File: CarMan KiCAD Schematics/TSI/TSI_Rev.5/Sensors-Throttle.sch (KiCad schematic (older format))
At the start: 56 parts, among them IC1 TS431ILT, J13 Conn_01x01, J22 Conn_01x01, J23 Conn_01x01, J24 Conn_01x01, J25 Conn_01x01, J26 J26, U21 MCP6004, U25 NCD9830DBR2G, U26 MCP6004, U4 ACPL-C870, U40 MCP6004, U5 SI8600AB-B-IS

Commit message: TSI Footprints - Res, Caps, Inductor all 0805s - Mounting Holes
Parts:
- C20, C21, C30, C32, C35, C4, C43, C46, C47, C48, C9: footprint (none) -> Capacitor_SMD:C_0805_2012Metric_Pad1.15x1.40mm_HandSolder
- R10, R103, R13, R16, R50, R51, R53, R58, R59, R6, R62, R63, R64, R66, R7, R76, R77, R78, R84, R85, R86, R87, R88, R89, R9, R90, R91, R93, R94, R95, R96: footprint (none) -> Resistor_SMD:R_0805_2012Metric_Pad1.15x1.40mm_HandSolder
- U40: footprint (none) -> TSI_Rev_2021_Footprint_Lib:SOIC127P600X175-14N

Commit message: TSI Footprinting (~80%)  - Added Molex  - Added Current Sensor
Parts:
- J13, J23, J24, J25, J26: footprint (none) -> Connector_PinHeader_1.00mm:PinHeader_1x01_P1.00mm_Vertical
- J22: value Conn_01x01 -> J22; footprint (none) -> Connector_PinHeader_1.00mm:PinHeader_1x01_P1.00mm_Vertical
- TP8: footprint (none) -> TestPoint:TestPoint_Pad_D3.0mm
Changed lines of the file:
@@
 F 0 "J24" V 14350 5650 50  0000 L CNN
 F 1 "Conn_01x01" V 14350 5500 50  0001 L CNN
-F 2 "" H 14250 5700 50  0001 C CNN
+F 2 "Connector_PinHeader_1.00mm:PinHeader_1x01_P1.00mm_Vertical" H 14250 5700 50  0001 C CNN
 F 3 "~" H 14250 5700 50  0001 C CNN
 	1    14250 5700
@@
 F 0 "J23" V 14350 4750 50  0000 L CNN
 F 1 "Conn_01x01" V 14213 4880 50  0001 L CNN
-F 2 "" H 14250 4800 50  0001 C CNN
+F 2 "Connector_PinHeader_1.00mm:PinHeader_1x01_P1.00mm_Vertical" H 14250 4800 50  0001 C CNN
 F 3 "~" H 14250 4800 50  0001 C CNN
 	1    14250 4800
@@
 F 0 "J25" V 14350 6450 50  0000 L CNN
 F 1 "Conn_01x01" V 14350 6300 50  0001 L CNN
-F 2 "" H 14250 6500 50  0001 C CNN
+F 2 "Connector_PinHeader_1.00mm:PinHeader_1x01_P1.00mm_Vertical" H 14250 6500 50  0001 C CNN
 F 3 "~" H 14250 6500 50  0001 C CNN
 	1    14250 6500
@@
 P 12800 6500
 F 0 "J22" V 12900 6450 50  0000 L CNN
-F 1 "Conn_01x01" V 12900 6300 50  0001 L CNN
-F 2 "" H 12800 6500 50  0001 C CNN
+F 1 "J22" V 12900 6300 50  0001 L CNN
+F 2 "Connector_PinHeader_1.00mm:PinHeader_1x01_P1.00mm_Vertical" H 12800 6500 50  0001 C CNN
 F 3 "~" H 12800 6500 50  0001 C CNN
 	1    12800 6500
@@
 F 0 "J26" V 12900 5650 50  0000 L CNN
 F 1 "J26" V 12900 5500 50  0001 L CNN
-F 2 "" H 12800 5700 50  0001 C CNN
+F 2 "Connector_PinHeader_1.00mm:PinHeader_1x01_P1.00mm_Vertical" H 12800 5700 50  0001 C CNN
 F 3 "~" H 12800 5700 50  0001 C CNN
 	1    12800 5700
@@
 F 0 "J13" V 12900 4750 50  0000 L CNN
 F 1 "Conn_01x01" V 12900 4600 50  0001 L CNN
-F 2 "" H 12800 4800 50  0001 C CNN
+F 2 "Connector_PinHeader_1.00mm:PinHeader_1x01_P1.00mm_Vertical" H 12800 4800 50  0001 C CNN
 F 3 "~" H 12800 4800 50  0001 C CNN
 	1    12800 4800
@@
 F 0 "TP8" H 6850 2050 50  0000 L CNN
 F 1 "Throttle_HV" H 6600 2250 50  0000 L CNN
-F 2 "" H 7000 2000 50  0001 C CNN
+F 2 "TestPoint:TestPoint_Pad_D3.0mm" H 7000 2000 50  0001 C CNN
 F 3 "~" H 7000 2000 50  0001 C CNN
 	1    6800 2000

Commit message: Started TSI PCB
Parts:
- removed unit 1 of U26
- added unit 4 of U26
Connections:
- net MC_Voltage: now also U21.7; no longer U21.1
- net TSV_Voltage: now also U21.1; no longer U21.7
- net at R95.1: now also U26.13 (-), U26.14
- net at C4.1, J13.1 (Pin_1), R6.2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: now also U26.12 (+)
- net at R95.2: now also U21.6 (-); no longer U21.2 (-)
- net at R89.1, R96.2: now also U21.5 (+); no longer U21.3 (+)
- net at R91.2, R93.2: now also U21.3 (+); no longer U21.5 (+)
- net at R90.1, R94.2: now also U21.2 (-); no longer U21.6 (-)
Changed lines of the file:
@@
 $Descr A3 16535 11693
 encoding utf-8
-Sheet 6 6
+Sheet 5 6
 Title ""
 Date ""
@@
 Wire Wire Line
 	10900 4300 11000 4300
-Text Notes 11700 4200 2    55   ~ 0
+Text Notes 11600 4150 2    55   ~ 0
 Bypass Cap for U26\n\n
 Wire Wire Line
@@
 $Comp
 L Amplifier_Operational:MCP6004 U21
-U 1 1 5F995327
+U 2 1 5F995327
 P 10000 5100
 F 0 "U21" H 10000 5100 50  0000 C CNN
@@
 F 2 "TSI_Rev_2021_Footprint_Lib:SOIC127P600X175-14N" H 9950 5200 50  0001 C CNN
 F 3 "http://ww1.microchip.com/downloads/en/DeviceDoc/21733j.pdf" H 10050 5300 50  0001 C CNN
-	1    10000 5100
+	2    10000 5100
 	-1   0    0    1
 $EndComp
@@
 $Comp
 L Amplifier_Operational:MCP6004 U21
-U 2 1 5F995FD0
+U 1 1 5F995FD0
 P 10000 6300
 F 0 "U21" H 10000 6300 50  0000 C CNN
@@
 F 2 "TSI_Rev_2021_Footprint_Lib:SOIC127P600X175-14N" H 9950 6400 50  0001 C CNN
 F 3 "http://ww1.microchip.com/downloads/en/DeviceDoc/21733j.pdf" H 10050 6500 50  0001 C CNN
-	2    10000 6300
+	1    10000 6300
 	-1   0    0    -1
 $EndComp
@@
 Text HLabel 2100 9200 0    50   Input ~ 0
 Throttle_LV
-Text HLabel 5950 9700 2    50   Output ~ 0
+Text HLabel 5950 9750 2    50   Output ~ 0
 1.24V_REF
 Text HLabel 5750 8800 0    50   Input ~ 0
@@
 Text HLabel 5750 8700 0    50   Input ~ 0
 5HV
-Text HLabel 5750 9300 0    50   Input ~ 0
+Text HLabel 5750 9400 0    50   Input ~ 0
 Throttle_HV
 Wire Wire Line
@@
 IO_Ground
 Wire Wire Line
-	5950 9300 5750 9300
-Text Label 5950 9300 0    50   ~ 0
+	5950 9400 5750 9400
+Text Label 5950 9400 0    50   ~ 0
 Throttle_HV
 Wire Wire Line
 	5950 8700 5750 8700
 Wire Wire Line
-	5950 9700 5750 9700
-Text Label 5750 9700 2    50   ~ 0
+	5950 9750 5750 9750
+Text Label 5750 9750 2    50   ~ 0
 DiffAmp_REF
 Text Label 5950 8700 0    50   ~ 0
@@
 Text Notes 5150 8550 0    79   ~ 0
 HIGH VOLTAGE SIGNALS\n
+Text Label 5950 9200 0    50   ~ 0
+HV+
+Wire Wire Line
+	5950 9200 5750 9200
+Text Label 5950 8900 0    50   ~ 0
+TSV_Voltage
 Text Label 5950 9100 0    50   ~ 0
+MC+
+Wire Wire Line
+	5950 9100 5750 9100
+Wire Wire Line
+	5950 8900 5750 8900
+Text HLabel 5750 8900 0    50   Input ~ 0
+TSV_Voltage
+Text HLabel 5750 9100 0    50   Input ~ 0
+MC+
+Text HLabel 5750 9200 0    50   Input ~ 0
 HV+
-Wire Wire Line
-	5950 9100 5750 9100
-Text Label 5950 9000 0    50   ~ 0
-TSV_Voltage
-Text Label 5950 8900 0    50   ~ 0
-MC_Voltage
-Wire Wire Line
-	5950 8900 5750 8900
-Wire Wire Line
-	5950 9000 5750 9000
-Text HLabel 5750 9000 0    50   Input ~ 0
-TSV_Voltage
-Text HLabel 5750 8900 0    50   Input ~ 0
-MC_Voltage
-Text HLabel 5750 9100 0    50   Input ~ 0
-HV+
-Text Label 5950 9200 0    50   ~ 0
+Text Label 5950 9300 0    50   ~ 0
 HV-
 Wire Wire Line
-	5950 9200 5750 9200
-Text HLabel 5750 9200 0    50   Input ~ 0
+	5950 9300 5750 9300
+Text HLabel 5750 9300 0    50   Input ~ 0
 HV-
 Wire Notes Line
@@
 Text Notes 12100 10450 0    157  ~ 0
 V/I\n& THROTTLE VOLTAGE ISOLATOR
+Text Label 5950 9600 0    50   ~ 0
+A2_HV
 Text Label 5950 9500 0    50   ~ 0
+A1_HV
+Wire Wire Line
+	5950 9600 5750 9600
+Wire Wire Line
+	5950 9500 5750 9500
+Text HLabel 5750 9500 0    50   Input ~ 0
+A1_HV
+Text HLabel 5750 9600 0    50   Input ~ 0
 A2_HV
-Text Label 5950 9400 0    50   ~ 0
-A1_HV
-Wire Wire Line
-	5950 9500 5750 9500
-Wire Wire Line
-	5950 9400 5750 9400
-Text HLabel 5750 9400 0    50   Input ~ 0
-A1_HV
-Text HLabel 5750 9500 0    50   Input ~ 0
-A2_HV
-Wire Notes Line
-	5050 9800 6650 9800
+Wire Notes Line
+	5050 9850 6650 9850
 Wire Notes Line
 	5050 8350 5050 9800
@@
 Wire Notes Line
 	6650 8350 6650 9800
-$Comp
-L Amplifier_Operational:MCP6004 U26
-U 1 1 5F98F236
-P 11500 4700
-F 0 "U26" H 11500 4700 50  0000 C CNN
-F 1 "MCP6004" H 11650 4850 50  0000 C CNN
-F 2 "TSI_Rev_2021_Footprint_Lib:SOIC127P600X175-14N" H 11450 4800 50  0001 C CNN
-F 3 "http://ww1.microchip.com/downloads/en/DeviceDoc/21733j.pdf" H 11550 4900 50  0001 C CNN
-	1    11500 4700
-	-1   0    0    -1
-$EndComp
 $Comp
 L Amplifier_Operational:MCP6004 U26
@@
 Wire Wire Line
 	3300 1350 3200 1350
+Text Label 5950 9000 0    50   ~ 0
+MC_Voltage
+Wire Wire Line
+	5950 9000 5750 9000
+Text HLabel 5750 9000 0    50   Input ~ 0
+MC_Voltage
+$Comp
+L Amplifier_Operational:MCP6004 U26
+U 4 1 601D0B35
+P 11500 4700
+F 0 "U26" H 11450 4700 50  0000 C CNN
+F 1 "MCP6004" H 11650 4850 50  0000 C CNN
+F 2 "TSI_Rev_2021_Footprint_Lib:SOIC127P600X175-14N" H 11450 4800 50  0001 C CNN
+F 3 "http://ww1.microchip.com/downloads/en/DeviceDoc/21733j.pdf" H 11550 4900 50  0001 C CNN
+	4    11500 4700
+	-1   0    0    -1
+$EndComp
 $EndSCHEMATC

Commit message: TSI (~97%)
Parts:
- J27: renamed from J22; value J22 -> J27
- renumbered J23 to J28
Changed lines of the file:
@@
 	14250 5500 14200 5500
 $Comp
-L Connector_Generic:Conn_01x01 J23
+L Connector_Generic:Conn_01x01 J28
 U 1 1 5FA1321C
 P 14250 4800
-F 0 "J23" V 14350 4750 50  0000 L CNN
+F 0 "J28" V 14350 4750 50  0000 L CNN
 F 1 "Conn_01x01" V 14213 4880 50  0001 L CNN
 F 2 "Connector_PinHeader_1.00mm:PinHeader_1x01_P1.00mm_Vertical" H 14250 4800 50  0001 C CNN
@@
 $EndComp
 $Comp
-L Connector_Generic:Conn_01x01 J22
+L Connector_Generic:Conn_01x01 J27
 U 1 1 5FA19A24
 P 12800 6500
-F 0 "J22" V 12900 6450 50  0000 L CNN
-F 1 "J22" V 12900 6300 50  0001 L CNN
+F 0 "J27" V 12900 6450 50  0000 L CNN
+F 1 "J27" V 12900 6300 50  0001 L CNN
 F 2 "Connector_PinHeader_1.00mm:PinHeader_1x01_P1.00mm_Vertical" H 12800 6500 50  0001 C CNN
 F 3 "~" H 12800 6500 50  0001 C CNN

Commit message: Aesthetics
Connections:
- net 5HV: now also U25.10 (REF_IN/REF_OUT)
- no-connect marks 7 -> 6
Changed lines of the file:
@@
 Text Label 8200 5550 0    50   ~ 0
 A1_HV
-NoConn ~ 6850 5250
 Wire Wire Line
 	6750 6000 6850 6000
@@
 	-1   0    0    -1
 $EndComp
+Text Label 6550 5250 0    50   ~ 0
+5HV
+Wire Wire Line
+	6550 5250 6850 5250
 $EndSCHEMATC

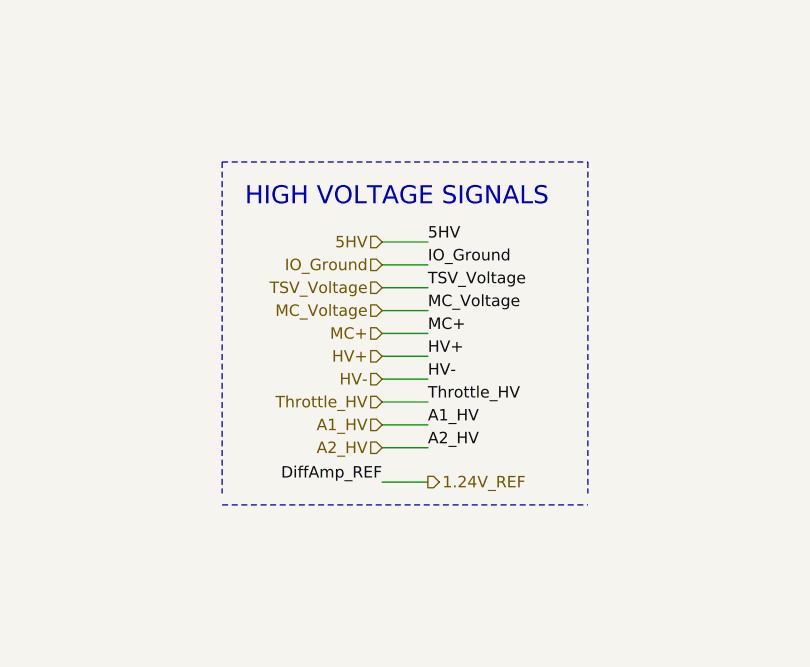
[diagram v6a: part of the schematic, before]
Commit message: TSI Signal Review ISSUES: - PCDC 'Pre_Charge_Ready' and 'PC_Ready' discrepancy - TSI Rev.4 IC1, IC4 -> PCDC & Isolators
REMOVED SIGNALS:
Throttle Plausibility
 - PC_Ready
 - Drive_BTN
 PCDC
 - HV+
 - HV-
 - Throttle_HV
 - IGNI_GND

STATUS LIGHTS & COCKPIT
- BP
- BP_RTN
- IMD_Status
- 5V
- Fault_LED
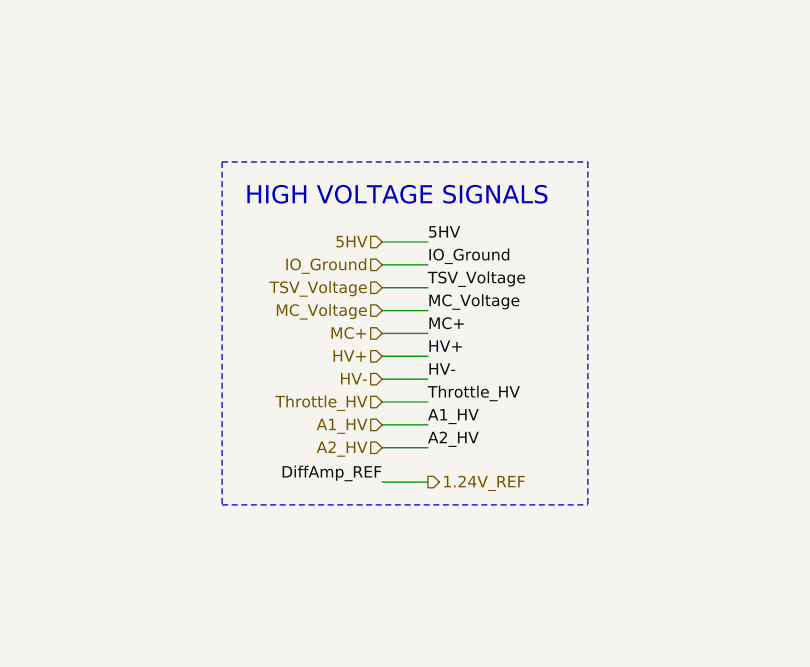
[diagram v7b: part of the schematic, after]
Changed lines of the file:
@@
 $Descr A3 16535 11693
 encoding utf-8
-Sheet 4 6
+Sheet 3 6
 Title ""
 Date ""
@@
 	5050 9850 6650 9850
 Wire Notes Line
-	5050 8350 5050 9800
-Wire Notes Line
 	5050 8350 6650 8350
-Wire Notes Line
-	6650 8350 6650 9800
 $Comp
 L Amplifier_Operational:MCP6004 U26
@@
 Wire Wire Line
 	6550 5250 6850 5250
+Wire Notes Line
+	6650 8350 6650 9850
+Wire Notes Line
+	5050 8350 5050 9850
 $EndSCHEMATC

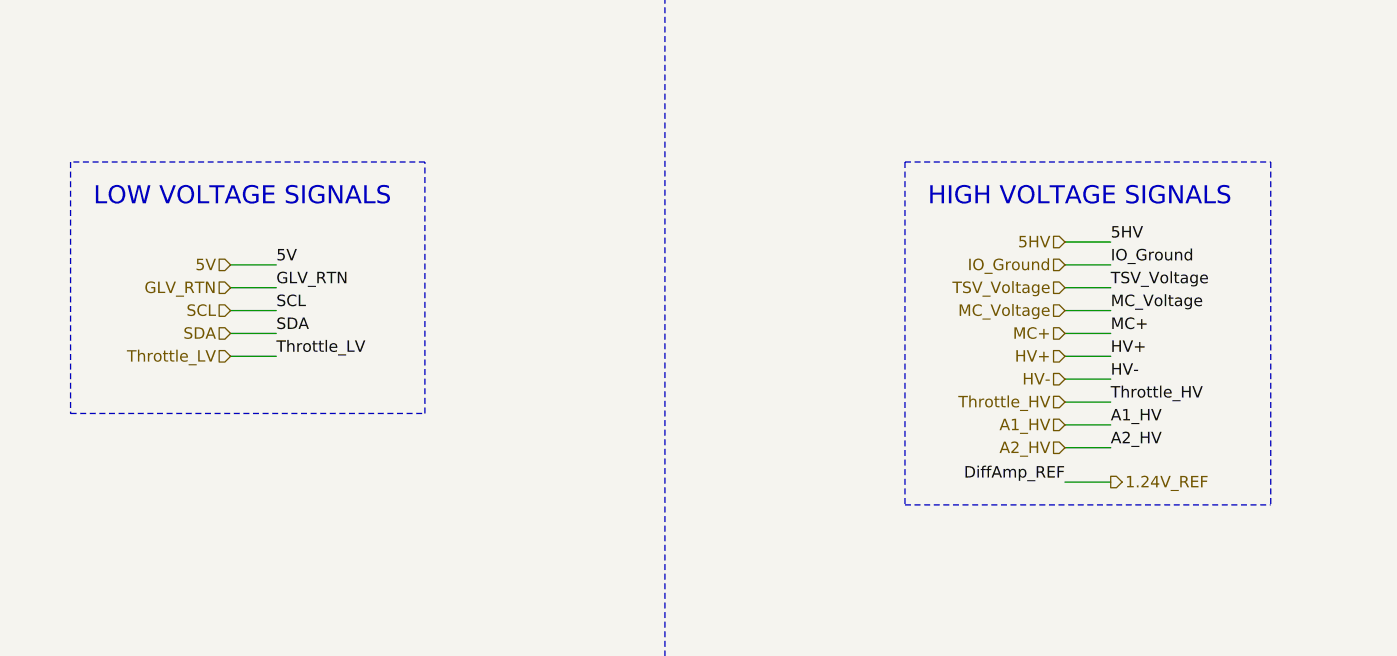
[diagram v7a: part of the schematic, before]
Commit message: Updated Signals and Trace Width
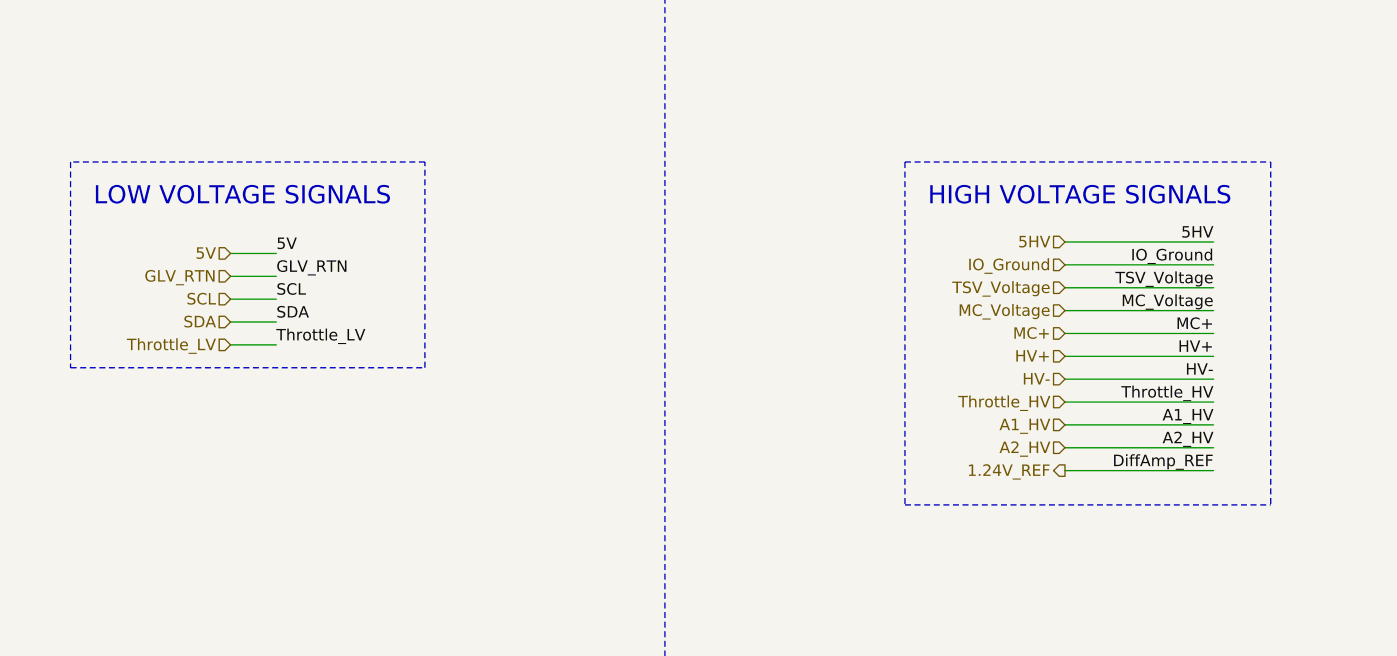
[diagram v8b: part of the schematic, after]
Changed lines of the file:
@@
 Text Notes 1500 8550 0    79   ~ 0
 LOW VOLTAGE SIGNALS\n
-Text Label 2300 8900 0    50   ~ 0
+Text Label 2300 8850 0    50   ~ 0
 GLV_RTN
 Wire Wire Line
-	2300 8900 2100 8900
-Text Label 2300 9200 0    50   ~ 0
+	2300 8850 2100 8850
+Text Label 2300 9150 0    50   ~ 0
 Throttle_LV
 Wire Wire Line
-	2300 9200 2100 9200
-Text Label 2300 8800 0    50   ~ 0
+	2300 9150 2100 9150
+Text Label 2300 8750 0    50   ~ 0
 5V
 Wire Wire Line
-	2300 8800 2100 8800
-Text HLabel 2100 8900 0    50   Input ~ 0
+	2300 8750 2100 8750
+Text HLabel 2100 8850 0    50   Input ~ 0
 GLV_RTN
-Text HLabel 2100 8800 0    50   Input ~ 0
+Text HLabel 2100 8750 0    50   Input ~ 0
 5V
-Text Label 2300 9100 0    50   ~ 0
+Text Label 2300 9050 0    50   ~ 0
 SDA
-Text Label 2300 9000 0    50   ~ 0
+Text Label 2300 8950 0    50   ~ 0
 SCL
 Wire Wire Line
-	2300 9000 2100 9000
-Wire Wire Line
-	2300 9100 2100 9100
-Text HLabel 2100 9100 0    50   Input ~ 0
+	2300 8950 2100 8950
+Wire Wire Line
+	2300 9050 2100 9050
+Text HLabel 2100 9050 0    50   Input ~ 0
 SDA
-Text HLabel 2100 9000 0    50   Input ~ 0
+Text HLabel 2100 8950 0    50   Input ~ 0
 SCL
-Text HLabel 2100 9200 0    50   Input ~ 0
+Text HLabel 2100 9150 0    50   Input ~ 0
 Throttle_LV
-Text HLabel 5950 9750 2    50   Output ~ 0
+Text HLabel 5750 9700 0    50   Output ~ 0
 1.24V_REF
 Text HLabel 5750 8800 0    50   Input ~ 0
@@
 Text HLabel 5750 9400 0    50   Input ~ 0
 Throttle_HV
-Wire Wire Line
-	5950 8800 5750 8800
-Text Label 5950 8800 0    50   ~ 0
+Text Label 6400 8800 2    50   ~ 0
 IO_Ground
-Wire Wire Line
-	5950 9400 5750 9400
-Text Label 5950 9400 0    50   ~ 0
+Text Label 6400 9400 2    50   ~ 0
 Throttle_HV
-Wire Wire Line
-	5950 8700 5750 8700
-Wire Wire Line
-	5950 9750 5750 9750
-Text Label 5750 9750 2    50   ~ 0
+Text Label 6400 9700 2    50   ~ 0
 DiffAmp_REF
-Text Label 5950 8700 0    50   ~ 0
-5HV
-Wire Notes Line
-	1400 9450 2950 9450
-Wire Notes Line
-	2950 9450 2950 8350
+Text Label 6400 8700 2    50   ~ 0
+5HV
+Wire Notes Line
+	1400 9250 2950 9250
 Wire Notes Line
 	2950 8350 1400 8350
-Wire Notes Line
-	1400 8350 1400 9450
 Text Notes 5150 8550 0    79   ~ 0
 HIGH VOLTAGE SIGNALS\n
-Text Label 5950 9200 0    50   ~ 0
+Text Label 6400 9200 2    50   ~ 0
 HV+
-Wire Wire Line
-	5950 9200 5750 9200
-Text Label 5950 8900 0    50   ~ 0
+Text Label 6400 8900 2    50   ~ 0
 TSV_Voltage
-Text Label 5950 9100 0    50   ~ 0
+Text Label 6400 9100 2    50   ~ 0
 MC+
-Wire Wire Line
-	5950 9100 5750 9100
-Wire Wire Line
-	5950 8900 5750 8900
 Text HLabel 5750 8900 0    50   Input ~ 0
 TSV_Voltage
@@
 Text HLabel 5750 9200 0    50   Input ~ 0
 HV+
-Text Label 5950 9300 0    50   ~ 0
+Text Label 6400 9300 2    50   ~ 0
 HV-
-Wire Wire Line
-	5950 9300 5750 9300
 Text HLabel 5750 9300 0    50   Input ~ 0
 HV-
@@
 Text Notes 12100 10450 0    157  ~ 0
 V/I\n& THROTTLE VOLTAGE ISOLATOR
-Text Label 5950 9600 0    50   ~ 0
+Text Label 6400 9600 2    50   ~ 0
 A2_HV
-Text Label 5950 9500 0    50   ~ 0
+Text Label 6400 9500 2    50   ~ 0
 A1_HV
-Wire Wire Line
-	5950 9600 5750 9600
-Wire Wire Line
-	5950 9500 5750 9500
 Text HLabel 5750 9500 0    50   Input ~ 0
 A1_HV
@@
 Wire Wire Line
 	3300 1350 3200 1350
-Text Label 5950 9000 0    50   ~ 0
+Text Label 6400 9000 2    50   ~ 0
 MC_Voltage
-Wire Wire Line
-	5950 9000 5750 9000
 Text HLabel 5750 9000 0    50   Input ~ 0
 MC_Voltage
@@
 Wire Notes Line
 	5050 8350 5050 9850
+Wire Wire Line
+	5750 8900 6400 8900
+Wire Wire Line
+	5750 8700 6400 8700
+Wire Wire Line
+	5750 8800 6400 8800
+Wire Wire Line
+	5750 9200 6400 9200
+Wire Wire Line
+	5750 9000 6400 9000
+Wire Wire Line
+	5750 9100 6400 9100
+Wire Wire Line
+	5750 9500 6400 9500
+Wire Wire Line
+	5750 9300 6400 9300
+Wire Wire Line
+	5750 9400 6400 9400
+Wire Wire Line
+	5750 9600 6400 9600
+Wire Wire Line
+	5750 9700 6400 9700
+Wire Notes Line
+	2950 9250 2950 8350
+Wire Notes Line
+	1400 8350 1400 9250
 $EndSCHEMATC
